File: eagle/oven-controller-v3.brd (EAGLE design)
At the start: 72.3 x 45.4 mm, 44 parts, among them Q1 FDV305N, Q2 FDV305N, Q3 FDV305N, Q4 FDV305N, U1 ARDUINO_SHIELDLONGPADS, U2 MAX31855, U3 MAX31855, U4 MAX31855, U5 MAX31855, U6 MAX31855, U7 SN74LVC1G139

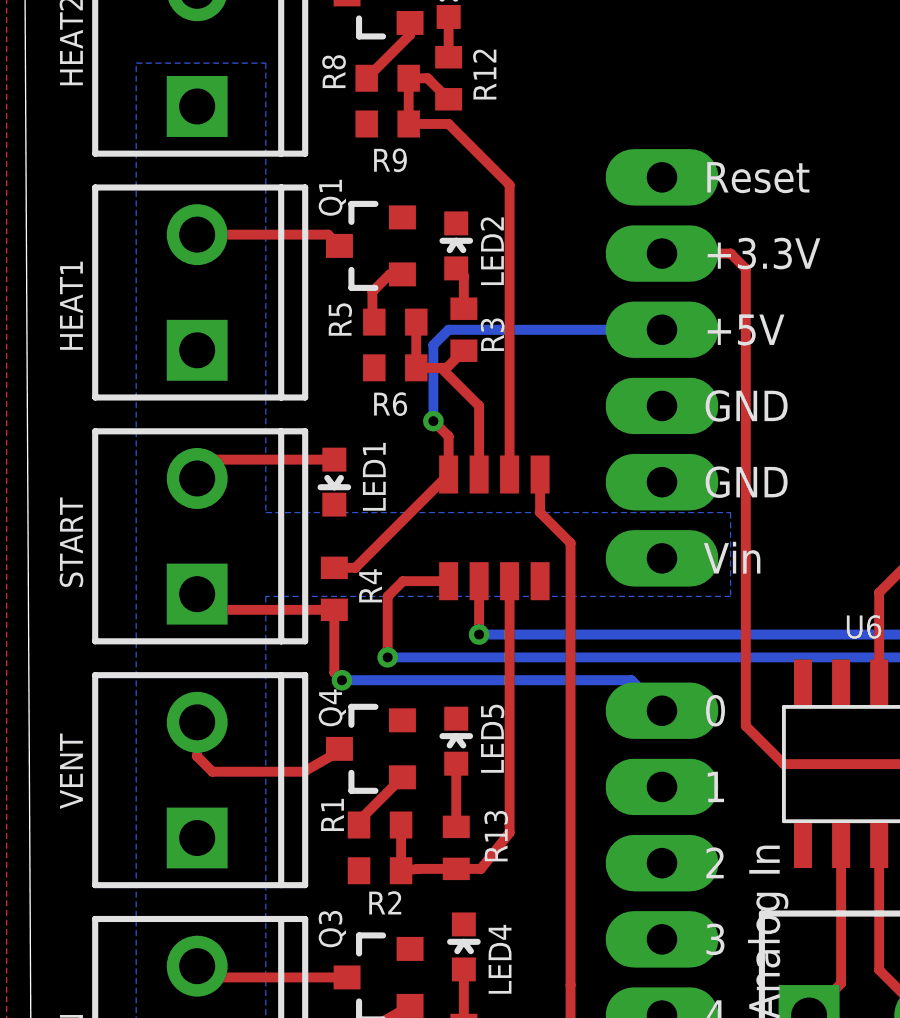
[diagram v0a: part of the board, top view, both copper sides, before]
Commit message: Changing directory structure.
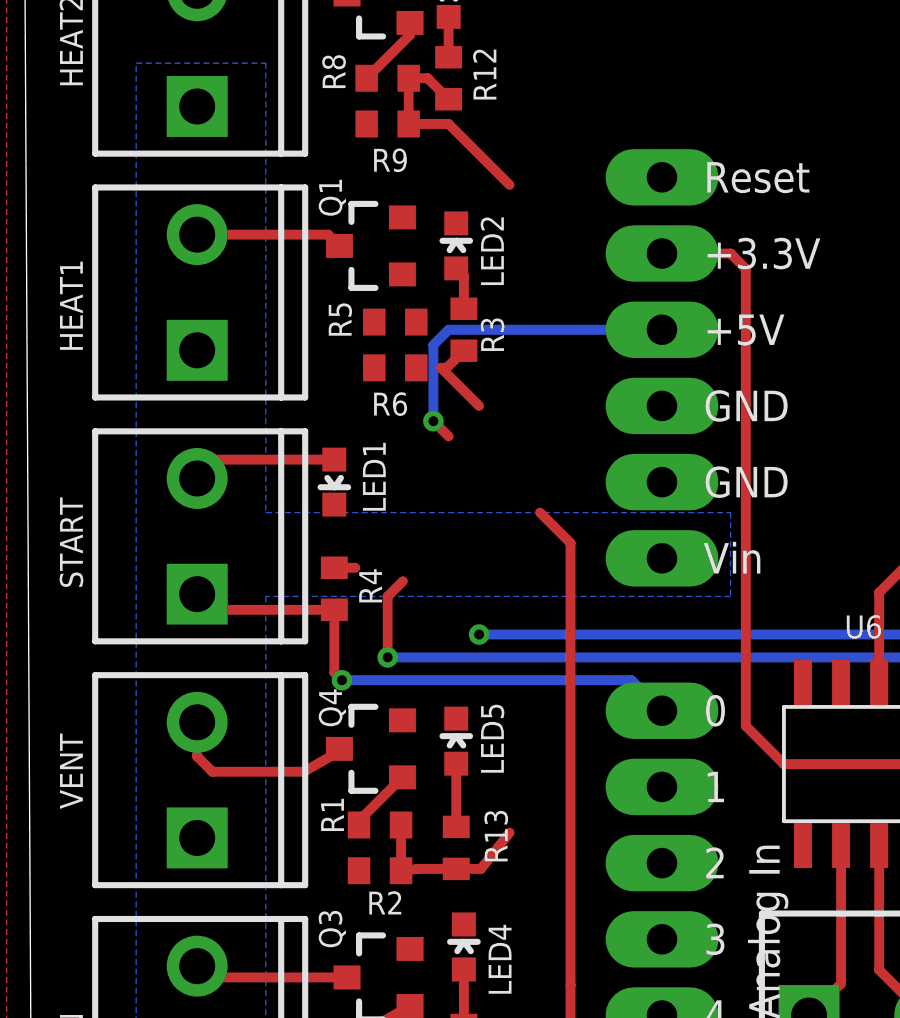
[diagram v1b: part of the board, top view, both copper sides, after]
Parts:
- removed U7: SN74LVC1G139, wicker:8LSSOP
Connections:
- removed net RELAY_MUX_SEL1: U1.D5, U7.P$1
- removed net RELAY_MUX_SEL2: U1.D6, U7.P$2
- net 5V: no longer U7.P$8
- net CS_FAN: now also U1.A1; no longer U7.P$5
- net CS_HEAT1: now also U1.D5; no longer R5.2, R6.2, U7.P$7
- net CS_HEAT2: now also U1.D6; no longer U7.P$6
- net CS_VENT: now also U1.A2; no longer U7.P$3
- net GND: no longer U7.P$4
- net N$1: now also R6.2
- net SPI_CLK: now also U2.5, U3.5, U4.5, U5.5, U6.5
- net SPI_MISO: now also U2.7, U3.7, U4.7, U5.7, U6.7
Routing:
- net RELAY_MUX_SEL1: track 62.5 -> 0.00 mm, vias 1 -> 0
- net CS_HEAT1: track 7.43 -> 63.8 mm, vias 0 -> 1
- net RELAY_MUX_SEL2: track 56.1 -> 0.00 mm, vias 1 -> 0
- net CS_HEAT2: track 17.0 -> 61.7 mm, vias 0 -> 1
- net CS_VENT: track 14.1 -> 5.73 mm
- net 5V: track 17.5 -> 11.8 mm
- net N$1: track 2.28 -> 0.00 mm
- net CS_FAN: track 26.6 -> 25.3 mm
